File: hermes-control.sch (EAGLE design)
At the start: 52 parts, among them Q1 600mA/40V, U1 LSM9DS1TR, U2 ESP32-WROOM-32D, U3 CP2104-F03-GM, U4 AP2112K-3.3TRG1, U5 MCP73831-2ACI/MC, U6 DMG3415U-7, U7 DMG3415U-7

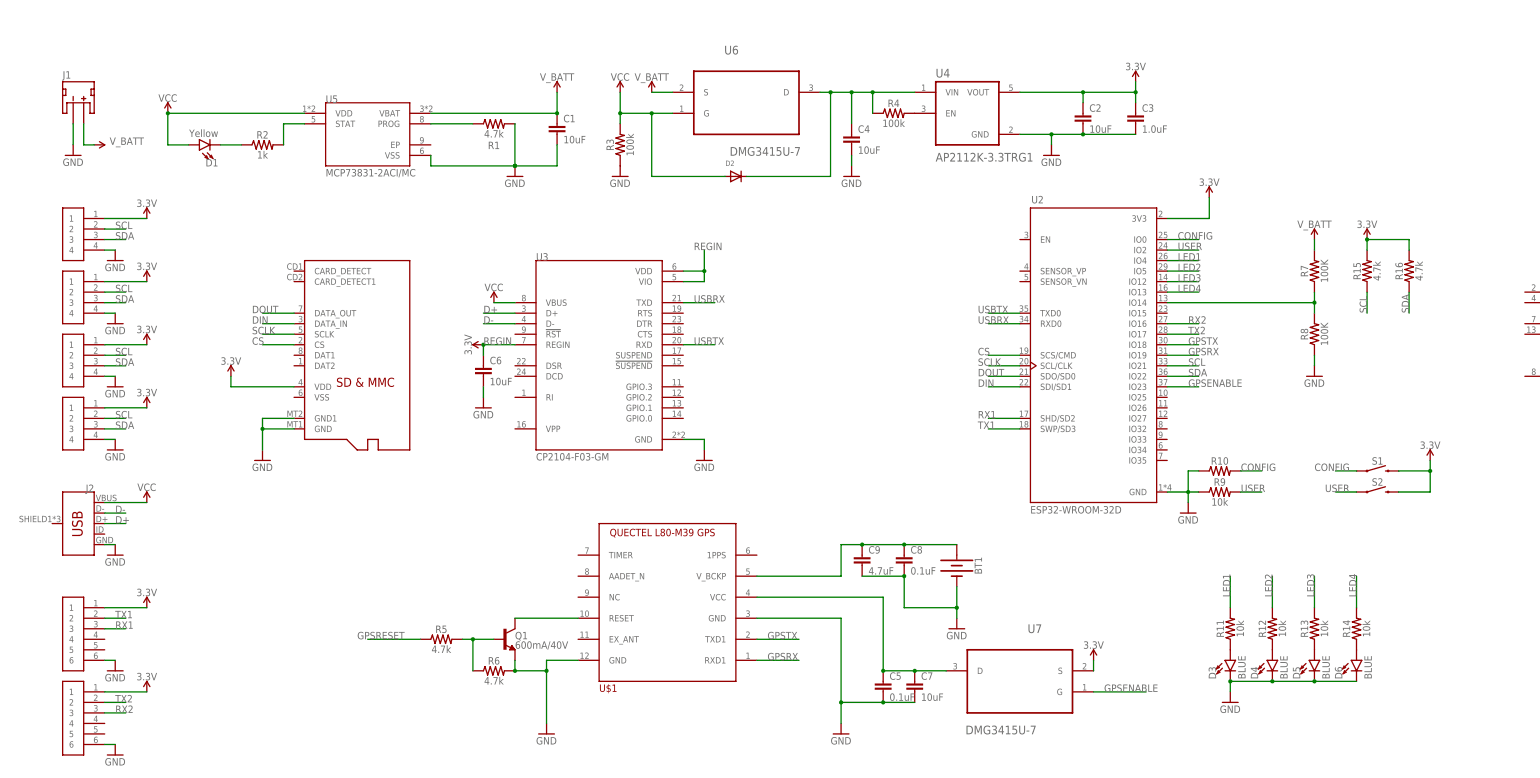
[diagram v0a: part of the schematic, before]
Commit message: updated componets to match bom
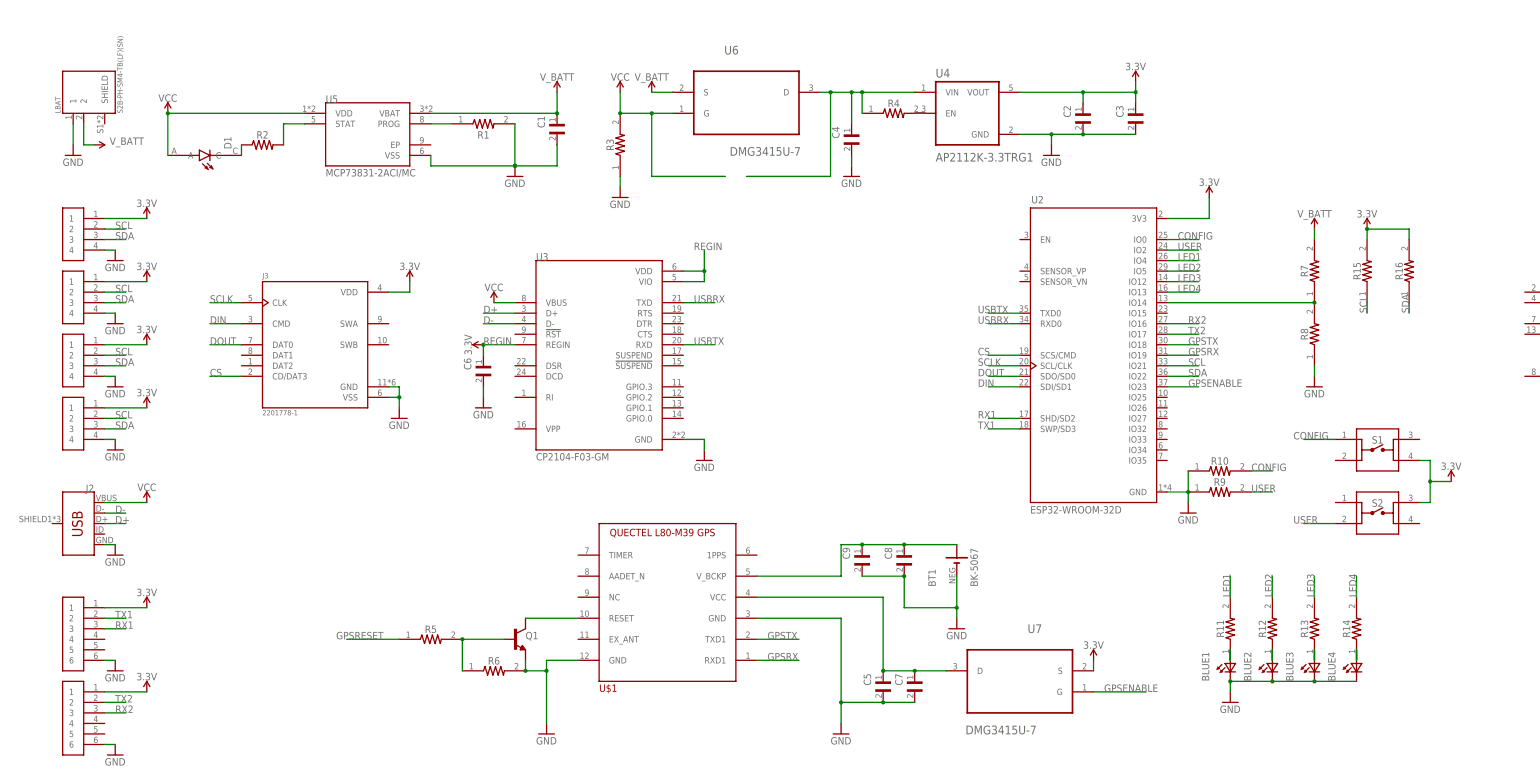
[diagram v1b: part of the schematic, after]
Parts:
- removed D2: (no value), adafruit:DIODESOD-123
- removed D3, D4, D5, D6: BLUE, SparkFun-LED:LED-BLUE1206
- removed J1: (no value), SparkFun-Connectors:JST_2MM_MALE
- removed U$2: MICROSD, adafruit:MICROSD
- added BLUE1, BLUE2, BLUE3, BLUE4: LTST-C190TBKT, hermes:LTST-C190TBKT
- added J3: 2201778-1, hermes:2201778-1
- added LBAT: S2B-PH-SM4-TB(LF)(SN), hermes:S2B-PH-SM4-TB(LF)(SN)
- BT1: value (none) -> BK-5067; device SparkFun-Batteries:BATTERY-12MM_SMD -> hermes:BK-5067
- C1, C2, C4, C6, C7: value 10uF -> EMK107BBJ106MA-T; device SparkFun-Capacitors:10UF-0805-10V-10% -> hermes:EMK107BBJ106MA-T
- C3: value 1.0uF -> GMK107AB7105KAHT; device SparkFun-Capacitors:1.0UF-0805-25V-(+80/-20%) -> hermes:GMK107AB7105KAHT
- C5, C8: value 0.1uF -> CL21B104KBCNNNC; device SparkFun-Capacitors:0.1UF-0603-25V-(+80/-20%) -> hermes:CL21B104KBCNNNC
- C9: value 4.7uF -> JMK107BJ475KA-T; device SparkFun-Capacitors:4.7UF0603 -> hermes:JMK107BJ475KA-T
- D1: device SparkFun-LED:LED-YELLOW0603 -> hermes:598-8040-107F
- Q1: value 600mA/40V -> MMBT2222A; device SparkFun-DiscreteSemi:TRANS_NPN-MMBT2222AL -> hermes:MMBT2222A
- R1, R15, R16, R5, R6: value 4.7k -> ERJ-XGNF4701Y; device SparkFun-Resistors:4.7KOHM-0603-1/10W-1% -> hermes:ERJ-XGNF4701Y
- R10, R11, R12, R13, R14, R9: value 10k -> RP73PF1J10KBTDF; device SparkFun-Resistors:10KOHM-0603-1/10W-1% -> hermes:RP73PF1J10KBTDF
- R2: value 1k -> CPF0402B1K0E1; device SparkFun-Resistors:1KOHM-0603-1/10W-1% -> hermes:CPF0402B1K0E1
- R3, R4: value 100k -> CPF0402B100KE1; device SparkFun-Resistors:100KOHM-0603-1/10W-1% -> hermes:CPF0402B100KE1
- R7, R8: value 100K -> CPF0402B100KE1; device SparkFun-Resistors:100KOHM-0402-1/16W-1% -> hermes:CPF0402B100KE1
- S1, S2: value MOMENTARY-SWITCH-SPST-PTH-6.0MM -> 1825910-7; device SparkFun-Switches:MOMENTARY-SWITCH-SPST-PTH-6.0MM -> hermes:1825910-7
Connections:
- removed net GND1: U$2.GND, U$2.GND1
- net 3.3V: now also J3.VDD, S1.4, S2.3; no longer S1.2, S2.2, U$2.VDD
- net CS: now also J3.CD/DAT3; no longer U$2.CS
- net DIN: now also J3.CMD; no longer U$2.DATA_IN
- net DOUT: now also J3.DAT0; no longer U$2.DATA_OUT
- net GND: now also BLUE1.K2, BLUE2.K2, BLUE3.K2, BLUE4.K2, BT1.N, J3.GND, J3.VSS, LBAT.1; no longer BT1.-, D3.C, D4.C, D5.C, D6.C, J1.-
- net N$11: now also BLUE1.A2; no longer D3.A
- net N$13: now also BLUE2.A2; no longer D4.A
- net N$14: now also BLUE3.A2; no longer D5.A
- net N$15: now also BLUE4.A2; no longer D6.A
- net N$4: no longer D2.C
- net N$7: now also BT1.P; no longer BT1.+
- net SCLK: now also J3.CLK; no longer U$2.SCLK
- net USER: now also S2.2; no longer S2.1
- net VCC: no longer D2.A
- net V_BATT: now also LBAT.2; no longer J1.+
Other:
- moved on the sheet: C1, C2, C3, C4, C5, C6, C7, C8, C9

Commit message: started to wries a few things
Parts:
- added C12, C14: CL21B104KBCNNNC, hermes:CL21B104KBCNNNC
- added C13: EMK107BBJ106MA-T, hermes:EMK107BBJ106MA-T
- added R17, R18, R19, R20: RP73PF1J10KBTDF, hermes:RP73PF1J10KBTDF
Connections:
- new net N$10: R18.2, U1.CS_M
- new net N$16: C14.1, U1.VDDIO
- new net N$17: R19.1, U1.SDO_A/G
- new net N$18: R20.1, U1.SDO_M
- new net N$9: R17.2, U1.CS_A/G
- net 3.3V: now also C12.1, C13.1, R17.1, R18.1, R19.2, R20.2, U1.VDD, U3.VBUS
- net GND: now also C12.2, C13.2, C14.2, U1.GND
- net SCL: now also U1.SCL/SPC
- net SDA: now also U1.SDA/SDI/SDO
- net VCC: no longer U3.VBUS
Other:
- moved on the sheet: BLUE1, BLUE2, BLUE3, BLUE4, BT1, C5, C7, C8, C9, Q1, R11, R12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

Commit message: it is done
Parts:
- added C10: GMK107AB7105KAHT, hermes:GMK107AB7105KAHT
- added Q2, Q3: MMBT2222A, hermes:MMBT2222A
- added R21, R22, R23: RP73PF1J10KBTDF, hermes:RP73PF1J10KBTDF
- added S3: 1825910-7, hermes:1825910-7
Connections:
- new net DTR: Q2.E, R22.2, U3.DTR
- new net ESP_RST: C10.1, Q3.C, R23.1, S3.1, U2.EN
- new net IO0: Q2.C, U2.IO0
- new net N$19: Q3.B, R22.1
- new net N$20: Q2.B, R21.1
- new net RTS: Q3.E, R21.2, U3.RTS
- net 3.3V: now also R23.2
- net CONFIG: now also U2.IO15; no longer U2.IO0
- net GND: now also C10.2, S3.4
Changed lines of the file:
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@@
 <part name="GND24" library="supply1" library_urn="urn:adsk.eagle:library:371" deviceset="GND" device=""/>
 <part name="SUPPLY9" library="SparkFun-PowerSymbols" library_urn="urn:adsk.eagle:library:530" deviceset="3.3V" device=""/>
+<part name="Q2" library="hermes" deviceset="MMBT2222A" device="" value="MMBT2222A"/>
+<part name="Q3" library="hermes" deviceset="MMBT2222A" device="" value="MMBT2222A"/>
+<part name="R21" library="hermes" deviceset="RP73PF1J10KBTDF" device="" value="RP73PF1J10KBTDF"/>
+<part name="R22" library="hermes" deviceset="RP73PF1J10KBTDF" device="" value="RP73PF1J10KBTDF"/>
+<part name="C10" library="hermes" deviceset="GMK107AB7105KAHT" device=""/>
+<part name="GND25" library="supply1" library_urn="urn:adsk.eagle:library:371" deviceset="GND" device=""/>
+<part name="S3" library="hermes" deviceset="1825910-7" device=""/>
+<part name="GND26" library="supply1" library_urn="urn:adsk.eagle:library:371" deviceset="GND" device=""/>
+<part name="SUPPLY25" library="SparkFun-PowerSymbols" library_urn="urn:adsk.eagle:library:530" deviceset="3.3V" device=""/>
+<part name="R23" library="hermes" deviceset="RP73PF1J10KBTDF" device="" value="RP73PF1J10KBTDF"/>
 </parts>
 <sheets>
@@
 <instance part="SUPPLY9" gate="G$1" x="149.86" y="124.46" smashed="yes">
 <attribute name="VALUE" x="149.86" y="127.254" size="1.778" layer="96" align="bottom-center"/>
+</instance>
+<instance part="Q2" gate="&gt;NAME" x="246.38" y="119.38" smashed="yes">
+<attribute name="NAME" x="248.92" y="119.38" size="1.778" layer="95" font="vector"/>
+</instance>
+<instance part="Q3" gate="&gt;NAME" x="246.38" y="101.6" smashed="yes" rot="MR180">
+<attribute name="NAME" x="248.92" y="101.6" size="1.778" layer="95" font="vector" rot="MR180"/>
+</instance>
+<instance part="R21" gate="G$1" x="233.68" y="119.38" smashed="yes" rot="R180">
+<attribute name="NAME" x="233.68" y="117.856" size="1.778" layer="95" font="vector" rot="R180" align="bottom-center"/>
+</instance>
+<instance part="R22" gate="G$1" x="233.68" y="101.6" smashed="yes" rot="R180">
+<attribute name="NAME" x="233.68" y="100.076" size="1.778" layer="95" font="vector" rot="R180" align="bottom-center"/>
+</instance>
+<instance part="C10" gate="G$1" x="358.14" y="154.94" smashed="yes" rot="R90">
+<attribute name="NAME" x="354.33" y="154.94" size="1.778" layer="95" rot="R90"/>
+<attribute name="VALUE" x="363.22" y="154.94" size="1.778" layer="96" rot="R90"/>
+</instance>
+<instance part="GND25" gate="1" x="358.14" y="147.32" smashed="yes">
+<attribute name="VALUE" x="355.6" y="144.78" size="1.778" layer="96"/>
+</instance>
+<instance part="S3" gate="G$1" x="398.78" y="73.66" smashed="yes">
+<attribute name="NAME" x="398.78" y="75.184" size="1.778" layer="95" font="vector" align="bottom-center"/>
+</instance>
+<instance part="GND26" gate="1" x="414.02" y="66.04" smashed="yes">
+<attribute name="VALUE" x="411.48" y="63.5" size="1.778" layer="96"/>
+</instance>
+<instance part="SUPPLY25" gate="G$1" x="360.68" y="78.74" smashed="yes">
+<attribute name="VALUE" x="360.68" y="81.534" size="1.778" layer="96" align="bottom-center"/>
+</instance>
+<instance part="R23" gate="G$1" x="375.92" y="76.2" smashed="yes" rot="R180">
+<attribute name="NAME" x="375.92" y="74.676" size="1.778" layer="95" font="vector" rot="R180" align="bottom-center"/>
 </instance>
 </instances>
@@
 <junction x="391.16" y="152.4"/>
 </segment>
+<segment>
+<pinref part="GND25" gate="1" pin="GND"/>
+<pinref part="C10" gate="G$1" pin="2"/>
+<wire x1="358.14" y1="149.86" x2="358.14" y2="152.4" width="0.1524" layer="91"/>
+</segment>
+<segment>
+<pinref part="S3" gate="G$1" pin="4"/>
+<pinref part="GND26" gate="1" pin="GND"/>
+<wire x1="408.94" y1="71.12" x2="414.02" y2="71.12" width="0.1524" layer="91"/>
+<wire x1="414.02" y1="71.12" x2="414.02" y2="68.58" width="0.1524" layer="91"/>
+</segment>
 </net>
 <net name="N$1" class="0">
@@
 <pinref part="U6" gate="A" pin="G"/>
 <wire x1="180.34" y1="172.72" x2="180.34" y2="167.64" width="0.1524" layer="91"/>
-<wire x1="180.34" y1="167.64" x2="187.96" y2="167.64" width="0.1524" layer="91"/>
+<wire x1="180.34" y1="167.64" x2="193.04" y2="167.64" width="0.1524" layer="91"/>
 <pinref part="R3" gate="G$1" pin="2"/>
-<wire x1="187.96" y1="167.64" x2="193.04" y2="167.64" width="0.1524" layer="91"/>
 <junction x="180.34" y="167.64"/>
-<wire x1="187.96" y1="167.64" x2="187.96" y2="152.4" width="0.1524" layer="91"/>
-<wire x1="187.96" y1="152.4" x2="205.74" y2="152.4" width="0.1524" layer="91"/>
-<junction x="187.96" y="167.64"/>
 </segment>
 <segment>
@@
 <wire x1="149.86" y1="124.46" x2="149.86" y2="121.92" width="0.1524" layer="91"/>
 </segment>
+<segment>
+<pinref part="R23" gate="G$1" pin="2"/>
+<pinref part="SUPPLY25" gate="G$1" pin="3.3V"/>
+<wire x1="368.3" y1="76.2" x2="360.68" y2="76.2" width="0.1524" layer="91"/>
+<wire x1="360.68" y1="76.2" x2="360.68" y2="78.74" width="0.1524" layer="91"/>
+</segment>
 </net>
 <net name="N$4" class="0">
@@
 <pinref part="U6" gate="A" pin="D"/>
 <pinref part="U4" gate="G$1" pin="VIN"/>
-<wire x1="228.6" y1="172.72" x2="231.14" y2="172.72" width="0.1524" layer="91"/>
-<wire x1="231.14" y1="172.72" x2="236.22" y2="172.72" width="0.1524" layer="91"/>
+<wire x1="228.6" y1="172.72" x2="236.22" y2="172.72" width="0.1524" layer="91"/>
 <wire x1="236.22" y1="172.72" x2="238.76" y2="172.72" width="0.1524" layer="91"/>
 <wire x1="238.76" y1="172.72" x2="251.46" y2="172.72" width="0.1524" layer="91"/>
-<wire x1="210.82" y1="152.4" x2="231.14" y2="152.4" width="0.1524" layer="91"/>
-<wire x1="231.14" y1="152.4" x2="231.14" y2="172.72" width="0.1524" layer="91"/>
-<junction x="231.14" y="172.72"/>
 <pinref part="C4" gate="G$1" pin="1"/>
 <wire x1="236.22" y1="165.1" x2="236.22" y2="172.72" width="0.1524" layer="91"/>
@@
 <net name="CONFIG" class="0">
 <segment>
-<pinref part="U2" gate="G$1" pin="IO0"/>
-<wire x1="312.42" y1="137.16" x2="320.04" y2="137.16" width="0.1524" layer="91"/>
-<label x="314.96" y="137.16" size="1.778" layer="95"/>
-</segment>
-<segment>
 <pinref part="R10" gate="G$1" pin="2"/>
 <wire x1="332.74" y1="81.28" x2="337.82" y2="81.28" width="0.1524" layer="91"/>
@@
 <wire x1="345.44" y1="48.26" x2="337.82" y2="48.26" width="0.1524" layer="91"/>
 <label x="335.28" y="48.26" size="1.778" layer="95"/>
+</segment>
+<segment>
+<pinref part="U2" gate="G$1" pin="IO15"/>
+<wire x1="312.42" y1="119.38" x2="320.04" y2="119.38" width="0.1524" layer="91"/>
+<label x="317.5" y="119.38" size="1.778" layer="95"/>
 </segment>
 </net>
@@
 </segment>
 </net>
+<net name="DTR" class="0">
+<segment>
+<pinref part="U3" gate="G$1" pin="DTR"/>
+<wire x1="195.58" y1="116.84" x2="203.2" y2="116.84" width="0.1524" layer="91"/>
+<label x="200.66" y="116.84" size="1.778" layer="95"/>
+</segment>
+<segment>
+<pinref part="R22" gate="G$1" pin="2"/>
+<pinref part="Q2" gate="&gt;NAME" pin="E"/>
+<wire x1="226.06" y1="101.6" x2="226.06" y2="106.68" width="0.1524" layer="91"/>
+<wire x1="226.06" y1="106.68" x2="248.92" y2="114.3" width="0.1524" layer="91"/>
+<wire x1="226.06" y1="101.6" x2="226.06" y2="96.52" width="0.1524" layer="91"/>
+<junction x="226.06" y="101.6"/>
+<label x="220.98" y="96.52" size="1.778" layer="95"/>
+</segment>
+</net>
+<net name="RTS" class="0">
+<segment>
+<pinref part="U3" gate="G$1" pin="RTS"/>
+<wire x1="195.58" y1="119.38" x2="203.2" y2="119.38" width="0.1524" layer="91"/>
+<label x="200.66" y="119.38" size="1.778" layer="95"/>
+</segment>
+<segment>
+<pinref part="Q3" gate="&gt;NAME" pin="E"/>
+<wire x1="248.92" y1="106.68" x2="226.06" y2="114.3" width="0.1524" layer="91"/>
+<pinref part="R21" gate="G$1" pin="2"/>
+<wire x1="226.06" y1="114.3" x2="226.06" y2="119.38" width="0.1524" layer="91"/>
+<wire x1="226.06" y1="119.38" x2="226.06" y2="124.46" width="0.1524" layer="91"/>
+<junction x="226.06" y="119.38"/>
+<label x="220.98" y="124.46" size="1.778" layer="95"/>
+</segment>
+</net>
+<net name="ESP_RST" class="0">
+<segment>
+<pinref part="U2" gate="G$1" pin="EN"/>
+<wire x1="276.86" y1="137.16" x2="269.24" y2="137.16" width="0.1524" layer="91"/>
+<label x="264.16" y="137.16" size="1.778" layer="95"/>
+</segment>
+<segment>
+<pinref part="Q3" gate="&gt;NAME" pin="C"/>
+<wire x1="248.92" y1="96.52" x2="248.92" y2="91.44" width="0.1524" layer="91"/>
+<label x="236.22" y="91.44" size="1.778" layer="95"/>
+</segment>
+<segment>
+<pinref part="C10" gate="G$1" pin="1"/>
+<wire x1="358.14" y1="160.02" x2="358.14" y2="167.64" width="0.1524" layer="91"/>
+<label x="345.44" y="162.56" size="1.778" layer="95"/>
+</segment>
+<segment>
+<pinref part="R23" gate="G$1" pin="1"/>
+<pinref part="S3" gate="G$1" pin="1"/>
+<wire x1="383.54" y1="76.2" x2="388.62" y2="76.2" width="0.1524" layer="91"/>
+<label x="381" y="78.74" size="1.778" layer="95"/>
+</segment>
+</net>
+<net name="IO0" class="0">
+<segment>
+<pinref part="U2" gate="G$1" pin="IO0"/>
+<wire x1="312.42" y1="137.16" x2="320.04" y2="137.16" width="0.1524" layer="91"/>
+<label x="317.5" y="137.16" size="1.778" layer="95"/>
+</segment>
+<segment>
+<pinref part="Q2" gate="&gt;NAME" pin="C"/>
+<wire x1="248.92" y1="124.46" x2="248.92" y2="129.54" width="0.1524" layer="91"/>
+<label x="248.92" y="129.54" size="1.778" layer="95"/>
+</segment>
+</net>
+<net name="N$19" class="0">
+<segment>
+<pinref part="R22" gate="G$1" pin="1"/>
+<pinref part="Q3" gate="&gt;NAME" pin="B"/>
+<wire x1="241.3" y1="101.6" x2="243.84" y2="101.6" width="0.1524" layer="91"/>
+</segment>
+</net>
+<net name="N$20" class="0">
+<segment>
+<pinref part="R21" gate="G$1" pin="1"/>
+<pinref part="Q2" gate="&gt;NAME" pin="B"/>
+<wire x1="241.3" y1="119.38" x2="243.84" y2="119.38" width="0.1524" layer="91"/>
+</segment>
+</net>
